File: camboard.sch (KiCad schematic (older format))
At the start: 30 parts, among them J1 Conn_02x05_Odd_Even, SW1 SW_Push, U1 MK82FN256VLL15, U2 Serial-Flash, U3 Serial-Flash

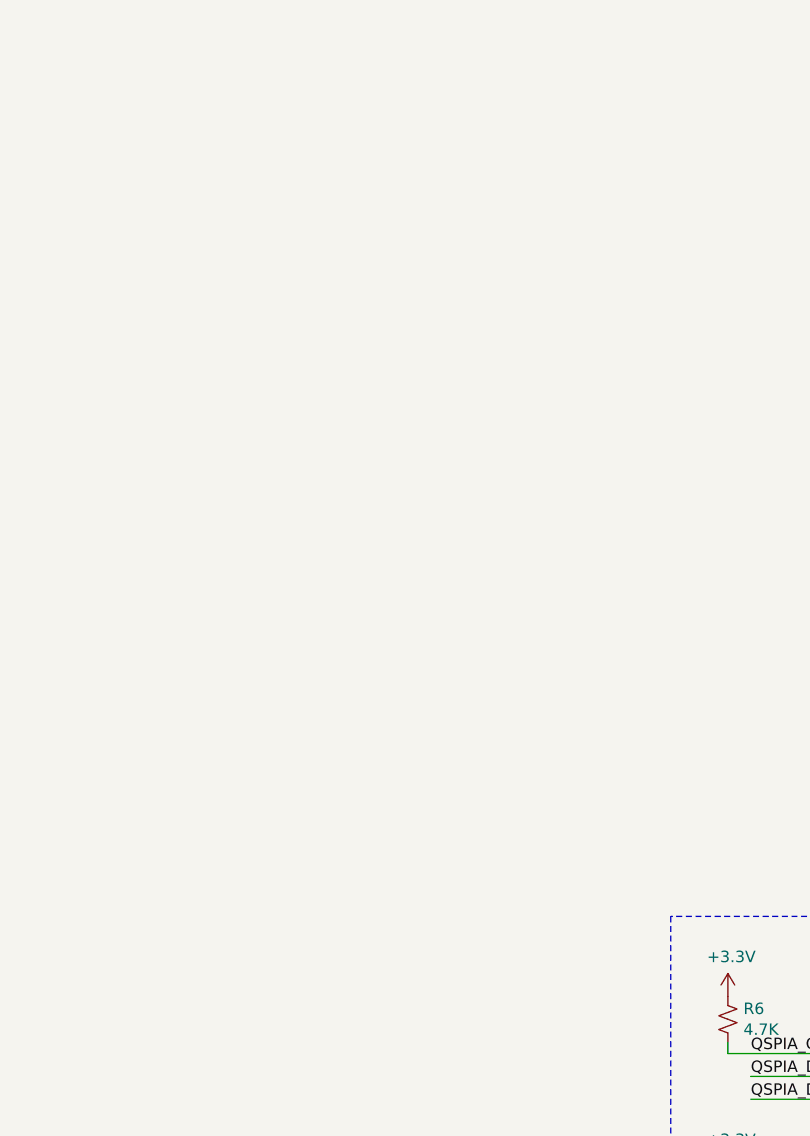
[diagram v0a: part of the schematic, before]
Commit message: Add FPC connector for display
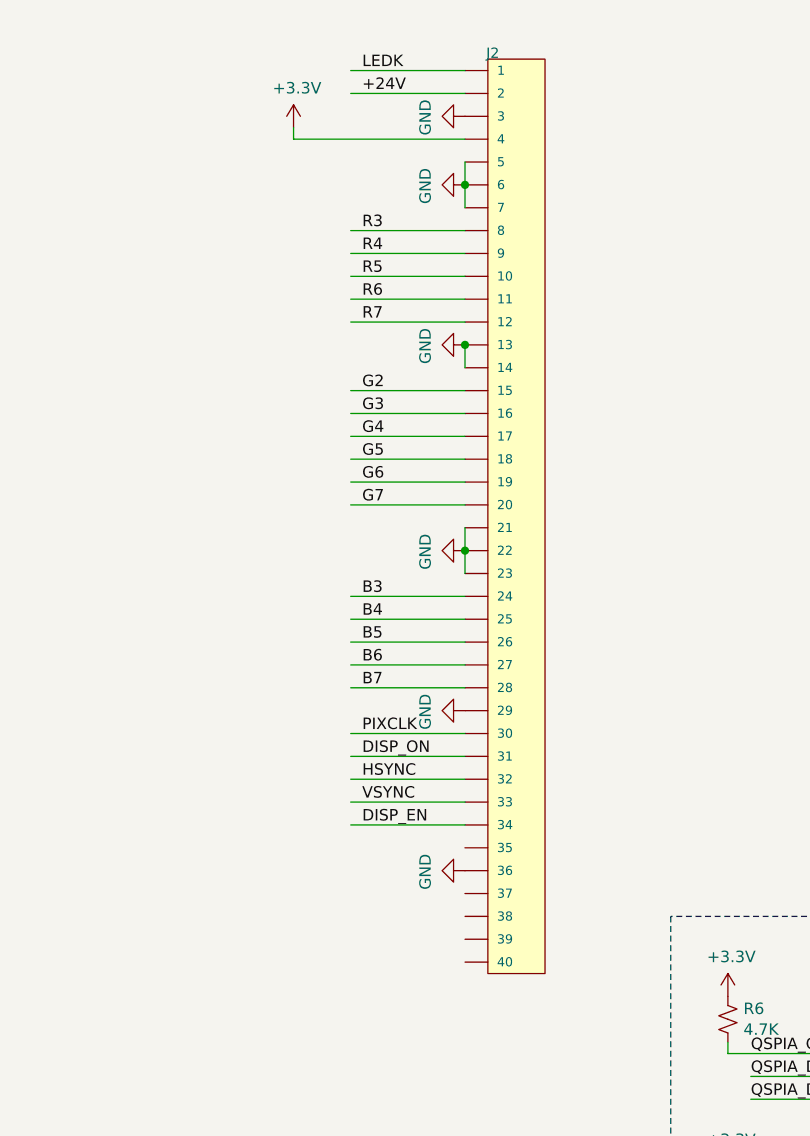
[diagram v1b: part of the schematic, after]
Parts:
- added J2: CONN_40, Connector_FFC-FPC:Hirose_FH12-40S-0.5SH_1x40-1MP_P0.50mm_Horizontal, symbol SparkFun-Connectors:CONN_40
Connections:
- net labels added: +24V, B3, B4, B5, B6, B7, DISP_EN, DISP_ON, G2, G3, G4, G5, G6, G7, HSYNC, LEDK, PIXCLK, R3, R4, R5, R6, R7, VSYNC
- wire segments 97 -> 127
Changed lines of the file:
@@
 Wire Wire Line
 	2700 6250 2800 6250
-Connection ~ 2800 6250
 Wire Wire Line
 	3600 5800 4000 5800
@@
 	1    0    0    -1
 $EndComp
-Connection ~ 2600 6800
 Text Label 3150 6800 0    50   ~ 0
 VDD
@@
 	2300 800  2400 800
 Connection ~ 2400 800
+$Comp
+L SparkFun-Connectors:CONN_40 J2
+U 1 1 5C721151
+P 7100 700
+F 0 "J2" H 7050 650 45  0000 L TNN
+F 1 "CONN_40" H 6823 2692 45  0001 R CNN
+F 2 "Connector_FFC-FPC:Hirose_FH12-40S-0.5SH_1x40-1MP_P0.50mm_Horizontal" H 7100 4800 20  0001 C CNN
+F 3 "" H 7100 700 50  0001 C CNN
+	1    7100 700
+	-1   0    0    1
+$EndComp
+Text Label 6550 700  0    50   ~ 0
+LEDK
+Wire Wire Line
+	6500 700  7000 700
+Text Label 6550 800  0    50   ~ 0
++24V
+Wire Wire Line
+	6500 800  7000 800
+Connection ~ 2800 6250
+$Comp
+L power:GND #PWR?
+U 1 1 5C7470F9
+P 7000 900
+F 0 "#PWR?" H 7000 650 50  0001 C CNN
+F 1 "GND" H 7005 727 50  0000 C CNN
+F 2 "" H 7000 900 50  0001 C CNN
+F 3 "" H 7000 900 50  0001 C CNN
+	1    7000 900
+	0    1    1    0
+$EndComp
+Connection ~ 2600 6800
+$Comp
+L power:+3.3V #PWR?
+U 1 1 5C75BA30
+P 6250 950
+F 0 "#PWR?" H 6250 800 50  0001 C CNN
+F 1 "+3.3V" H 6265 1123 50  0000 C CNN
+F 2 "" H 6250 950 50  0001 C CNN
+F 3 "" H 6250 950 50  0001 C CNN
+	1    6250 950
+	1    0    0    -1
+$EndComp
+Wire Wire Line
+	7000 1000 6250 1000
+Wire Wire Line
+	6250 1000 6250 950
+Wire Wire Line
+	7000 1100 7000 1200
+Connection ~ 7000 1200
+Wire Wire Line
+	7000 1200 7000 1300
+$Comp
+L power:GND #PWR?
+U 1 1 5C76F8C0
+P 7000 1200
+F 0 "#PWR?" H 7000 950 50  0001 C CNN
+F 1 "GND" H 7005 1027 50  0000 C CNN
+F 2 "" H 7000 1200 50  0001 C CNN
+F 3 "" H 7000 1200 50  0001 C CNN
+	1    7000 1200
+	0    1    1    0
+$EndComp
+Wire Wire Line
+	7000 1900 7000 2000
+$Comp
+L power:GND #PWR?
+U 1 1 5C77658F
+P 7000 1900
+F 0 "#PWR?" H 7000 1650 50  0001 C CNN
+F 1 "GND" H 7005 1727 50  0000 C CNN
+F 2 "" H 7000 1900 50  0001 C CNN
+F 3 "" H 7000 1900 50  0001 C CNN
+	1    7000 1900
+	0    1    1    0
+$EndComp
+Connection ~ 7000 1900
+Wire Wire Line
+	7000 2700 7000 2800
+Connection ~ 7000 2800
+Wire Wire Line
+	7000 2800 7000 2900
+$Comp
+L power:GND #PWR?
+U 1 1 5C77D33F
+P 7000 2800
+F 0 "#PWR?" H 7000 2550 50  0001 C CNN
+F 1 "GND" H 7005 2627 50  0000 C CNN
+F 2 "" H 7000 2800 50  0001 C CNN
+F 3 "" H 7000 2800 50  0001 C CNN
+	1    7000 2800
+	0    1    1    0
+$EndComp
+$Comp
+L power:GND #PWR?
+U 1 1 5C780B97
+P 7000 3500
+F 0 "#PWR?" H 7000 3250 50  0001 C CNN
+F 1 "GND" H 7005 3327 50  0000 C CNN
+F 2 "" H 7000 3500 50  0001 C CNN
+F 3 "" H 7000 3500 50  0001 C CNN
+	1    7000 3500
+	0    1    1    0
+$EndComp
+$Comp
+L power:GND #PWR?
+U 1 1 5C7842D8
+P 7000 4200
+F 0 "#PWR?" H 7000 3950 50  0001 C CNN
+F 1 "GND" H 7005 4027 50  0000 C CNN
+F 2 "" H 7000 4200 50  0001 C CNN
+F 3 "" H 7000 4200 50  0001 C CNN
+	1    7000 4200
+	0    1    1    0
+$EndComp
+Text Label 6550 1400 0    50   ~ 0
+R3
+Wire Wire Line
+	6500 1400 7000 1400
+Text Label 6550 1500 0    50   ~ 0
+R4
+Wire Wire Line
+	6500 1500 7000 1500
+Text Label 6550 1600 0    50   ~ 0
+R5
+Wire Wire Line
+	6500 1600 7000 1600
+Text Label 6550 1700 0    50   ~ 0
+R6
+Wire Wire Line
+	6500 1700 7000 1700
+Text Label 6550 1800 0    50   ~ 0
+R7
+Wire Wire Line
+	6500 1800 7000 1800
+Text Label 6550 2100 0    50   ~ 0
+G2
+Wire Wire Line
+	6500 2100 7000 2100
+Text Label 6550 2200 0    50   ~ 0
+G3
+Wire Wire Line
+	6500 2200 7000 2200
+Text Label 6550 2300 0    50   ~ 0
+G4
+Wire Wire Line
+	6500 2300 7000 2300
+Text Label 6550 2400 0    50   ~ 0
+G5
+Wire Wire Line
+	6500 2400 7000 2400
+Text Label 6550 2500 0    50   ~ 0
+G6
+Wire Wire Line
+	6500 2500 7000 2500
+Text Label 6550 2600 0    50   ~ 0
+G7
+Wire Wire Line
+	6500 2600 7000 2600
+Text Label 6550 3000 0    50   ~ 0
+B3
+Wire Wire Line
+	6500 3000 7000 3000
+Text Label 6550 3100 0    50   ~ 0
+B4
+Wire Wire Line
+	6500 3100 7000 3100
+Text Label 6550 3200 0    50   ~ 0
+B5
+Wire Wire Line
+	6500 3200 7000 3200
+Text Label 6550 3300 0    50   ~ 0
+B6
+Wire Wire Line
+	6500 3300 7000 3300
+Text Label 6550 3400 0    50   ~ 0
+B7
+Wire Wire Line
+	6500 3400 7000 3400
+Text Label 6550 3600 0    50   ~ 0
+PIXCLK
+Wire Wire Line
+	6500 3600 7000 3600
+Text Label 6550 3700 0    50   ~ 0
+DISP_ON
+Wire Wire Line
+	6500 3700 7000 3700
+Text Label 6550 3800 0    50   ~ 0
+HSYNC
+Wire Wire Line
+	6500 3800 7000 3800
+Text Label 6550 3900 0    50   ~ 0
+VSYNC
+Wire Wire Line
+	6500 3900 7000 3900
+Text Label 6550 4000 0    50   ~ 0
+DISP_EN
+Wire Wire Line
+	6500 4000 7000 4000
 $EndSCHEMATC
